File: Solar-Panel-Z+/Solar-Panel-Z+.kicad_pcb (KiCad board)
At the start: 6 copper layers, 48.4 x 48.4 mm, 79 parts, among them J1 FTS-105-01-L-DV-A, Q1 BSS138DWQ-7, Q2 MBT2222ADW1T1, Q3 BSS138DWQ-7, Q4 MBT2222ADW1T1, U1 BQ25570RGRR, U2 TSL2561

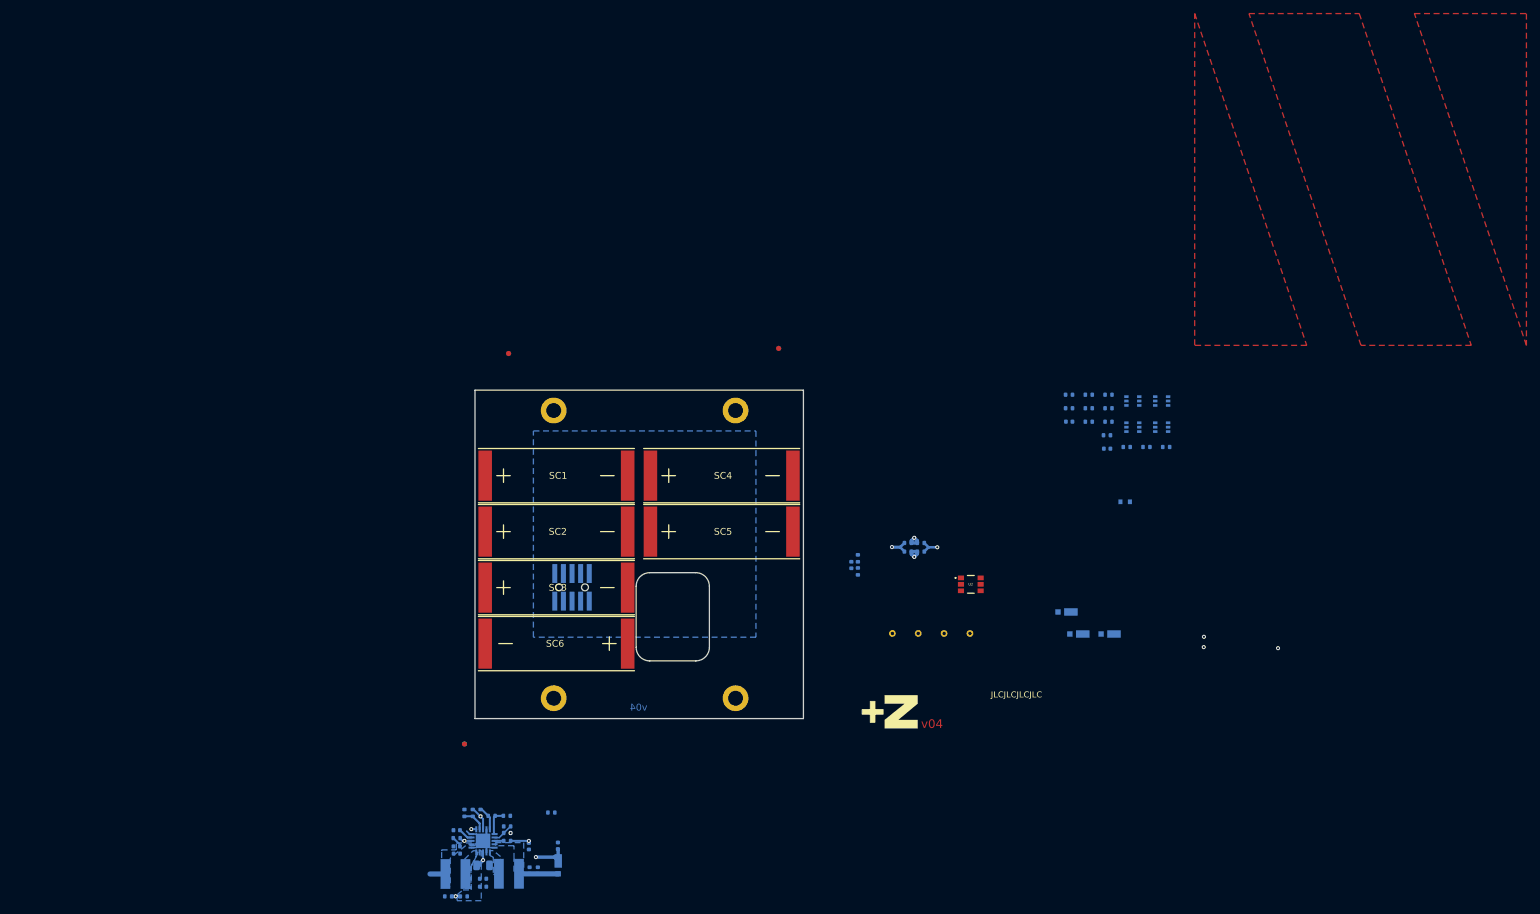
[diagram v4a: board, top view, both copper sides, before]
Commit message: Finish 6 Layer panel versions
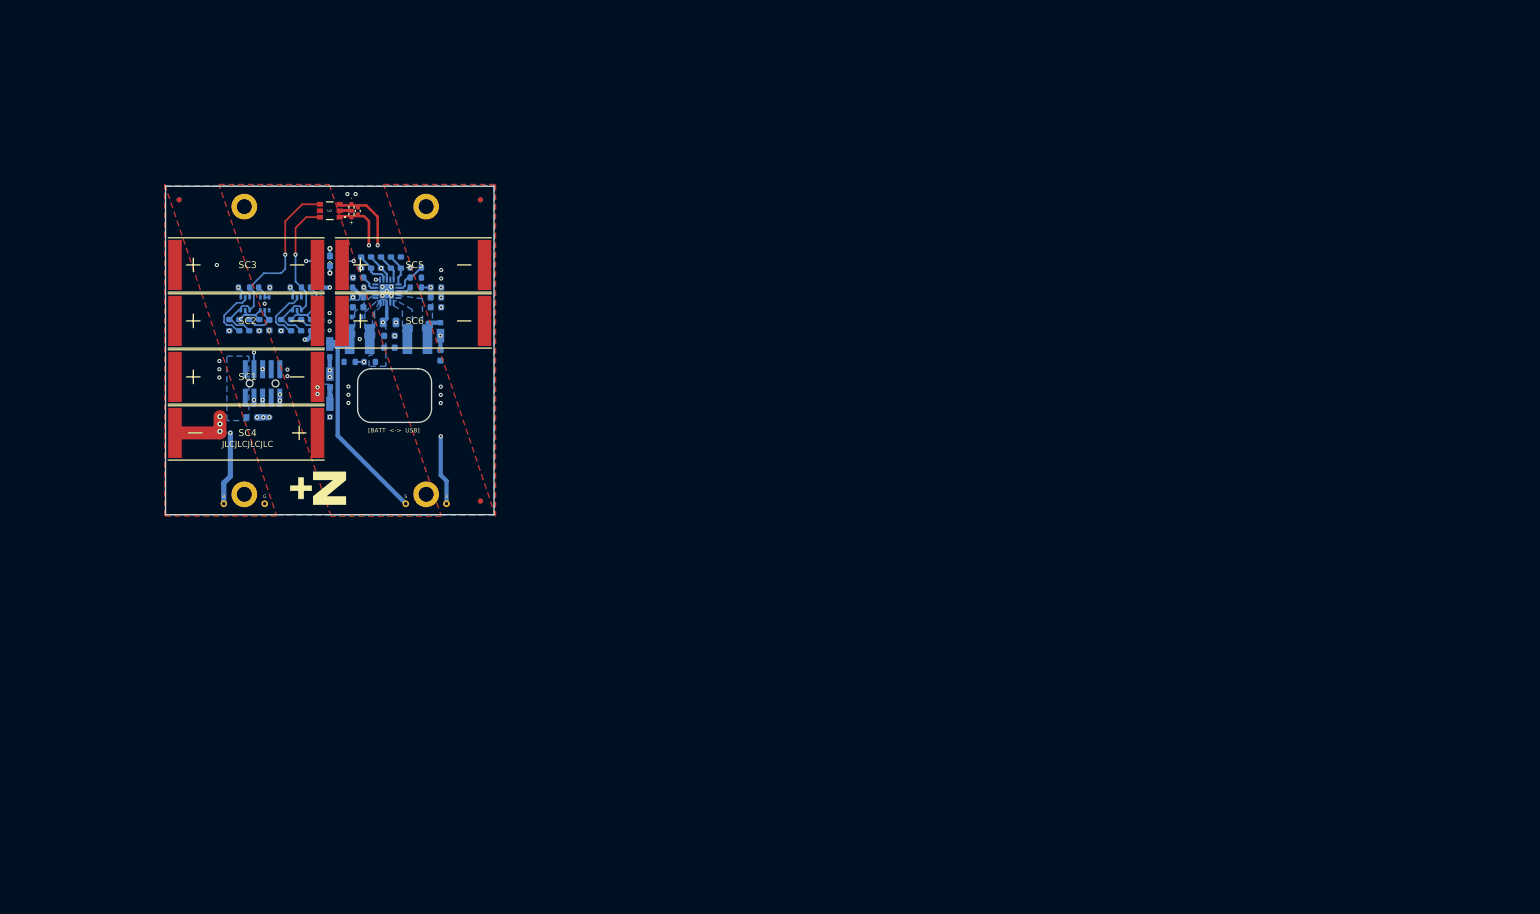
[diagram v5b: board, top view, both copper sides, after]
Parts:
- removed the C1 at (183.6, 98.1)
- removed R31: 200K, Resistor_SMD:R_0402_1005Metric
- removed the REF** at (133.1, 67.0) (x2)
- removed the REF** at (126.5, 124.5) (x2)
- removed the REF** at (172.8, 66.2) (x2)
- removed the Ref** at (143.9, 115.2)
- added C5: 100uF, Capacitor_SMD:C_0805_2012Metric, B.Cu at (115.5, 62.4)
- added R4: 0, Resistor_SMD:R_0603_1608Metric, B.Cu at (119.4, 57.2)
- added REF**: Fiducial_0.75mm_Mask1.5mm, Fiducial:Fiducial_0.75mm_Mask1.5mm, F.Cu at (128.9, 88.7)
- added REF**: Fiducial_0.75mm_Mask1.5mm, Fiducial:Fiducial_0.75mm_Mask1.5mm, F.Cu at (84.5, 44.3)
- added REF**: Fiducial_0.75mm_Mask1.5mm, Fiducial:Fiducial_0.75mm_Mask1.5mm, F.Cu at (128.9, 44.3)
- added REF**: Fiducial_0.75mm_Mask1.5mm, Fiducial:Fiducial_0.75mm_Mask1.5mm, B.Cu at (128.9, 44.3)
- added REF**: Fiducial_0.75mm_Mask1.5mm, Fiducial:Fiducial_0.75mm_Mask1.5mm, B.Cu at (84.5, 44.3)
- added REF**: Fiducial_0.75mm_Mask1.5mm, Fiducial:Fiducial_0.75mm_Mask1.5mm, B.Cu at (128.9, 88.7)
- added Ref**: Val**, custom-footprints:pycubed_mini_half, B.Cu at (106.2, 44.6)
- C1: renamed from C5; value 100uF -> 1uF; footprint Capacitor_SMD:C_0805_2012Metric -> Capacitor_SMD:C_0402_1005Metric; moved to F.Cu
- C10, C11, C12, C13, C2, C3, C4, C6, C7, C8, C9: footprint Capacitor_SMD:C_0402_1005Metric -> Capacitor_SMD:C_0603_1608Metric
- H1, H2, H3, H4: moved to B.Cu
- J1: footprint batteryboard:FTS-105-XX-YY-DV-A -> solarpanels:SAMTEC-FTS-105-01-X-DV-A
- R1, R2: moved to F.Cu
- R10, R11, R12, R13, R16, R17, R18, R24, R29, R3, R5, R6, R7, R8, R9: footprint Resistor_SMD:R_0402_1005Metric -> Resistor_SMD:R_0603_1608Metric
- R14, R15, R19: value 0 -> DNI; footprint Resistor_SMD:R_0402_1005Metric -> Resistor_SMD:R_0603_1608Metric
- R20: value 680 -> DNI; footprint Resistor_SMD:R_0402_1005Metric -> Resistor_SMD:R_0603_1608Metric
- R21: value 100K -> 680; footprint Resistor_SMD:R_0402_1005Metric -> Resistor_SMD:R_0603_1608Metric
- R22: value 0 -> 100K; footprint Resistor_SMD:R_0402_1005Metric -> Resistor_SMD:R_0603_1608Metric
- R23: value 0 -> 10K; footprint Resistor_SMD:R_0402_1005Metric -> Resistor_SMD:R_0603_1608Metric
- R25, R30: value 10K -> 200K; footprint Resistor_SMD:R_0402_1005Metric -> Resistor_SMD:R_0603_1608Metric
- R26: value 200K -> 680; footprint Resistor_SMD:R_0402_1005Metric -> Resistor_SMD:R_0603_1608Metric
- R27: value 680 -> 100K; footprint Resistor_SMD:R_0402_1005Metric -> Resistor_SMD:R_0603_1608Metric
- R28: value 100K -> 10K; footprint Resistor_SMD:R_0402_1005Metric -> Resistor_SMD:R_0603_1608Metric
- SC1, SC2, SC3, SC4, SC5, SC6: value SolarCell -> SolarCell_Small
- moved R21 137.8 mm to (93.4, 62.8), turned to 90 degrees
- moved Q1 133.4 mm to (97.1, 59.6), turned to -90 degrees
- moved Q2 132.1 mm to (94.2, 59.6), turned to -90 degrees
- moved R24 130.0 mm to (91.9, 62.8), turned to 90 degrees
- moved Q4 128.2 mm to (101.9, 59.6), turned to -90 degrees
- moved R22 126.1 mm to (97.0, 57.2)
- moved R20 124.7 mm to (101.7, 57.2)
- moved R23 122.9 mm to (96.3, 62.8), turned to 90 degrees
- moved R29 122.6 mm to (99.5, 62.8), turned to 90 degrees
- moved R25 121.4 mm to (94.8, 62.8), turned to 90 degrees
- moved Q3 121.1 mm to (104.8, 59.6), turned to -90 degrees
- moved D3 119.6 mm to (106.7, 75.1), turned to -90 degrees
- moved C12 118.7 mm to (97.8, 62.8), turned to -90 degrees
- moved R28 118.4 mm to (104.0, 62.8), turned to 90 degrees
- moved D5 118.1 mm to (106.7, 66.2), turned to -90 degrees
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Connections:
- C1 pad 1: VBAT -> GND
- C1 pad 2: GND -> +3V3
- J1 pad 10: VUSB -> BATT_P
- J1 pad 4: BURN2 -> GND
- J1 pad 7: SDA2 -> SDA
- J1 pad 8: SCL2 -> SCL
- Q2 pad 1: SCL2 -> SCL
- Q2 pad 3: SCL2 -> SCL
- Q4 pad 1: SDA2 -> SDA
- Q4 pad 3: SDA2 -> SDA
- R19 pad 1: VBAT_OK -> SCL_LS
- R19 pad 2: VOUT_EN -> SCL
- R20 pad 1: Net-(Q2-Pad2) -> SDA_LS
- R20 pad 2: Net-(Q1-Pad6) -> SDA
- R21 pad 1: +3V3 -> Net-(Q2-Pad2)
- R21 pad 2: Net-(Q1-Pad2) -> Net-(Q1-Pad6)
- R22 pad 1: SCL_LS -> +3V3
- R22 pad 2: SCL2 -> Net-(Q1-Pad2)
- R23 pad 1: SDA_LS -> +3V3
- R23 pad 2: SDA2 -> Net-(Q1-Pad6)
- R24 pad 2: Net-(Q1-Pad6) -> SCL_LS
- R25 pad 1: +3V3 -> SCL_LS
- R25 pad 2: SCL_LS -> Net-(C12-Pad1)
- R26 pad 1: SCL_LS -> Net-(Q4-Pad2)
- R26 pad 2: Net-(C12-Pad1) -> Net-(Q3-Pad6)
- R27 pad 1: Net-(Q4-Pad2) -> +3V3
- R27 pad 2: Net-(Q3-Pad6) -> Net-(Q3-Pad2)
- R28 pad 2: Net-(Q3-Pad2) -> Net-(Q3-Pad6)
- R29 pad 2: Net-(Q3-Pad6) -> SDA_LS
- R30 pad 1: +3V3 -> SDA_LS
- R30 pad 2: SDA_LS -> Net-(C13-Pad1)
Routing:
- net GND: track 13526.1 -> 20.8 mm, vias 3 -> 34
- net /coil: track 7.26 -> 13196.6 mm, vias 2 -> 5
- net SCL_LS: track 0.00 -> 31.3 mm, vias 0 -> 1
- net VSOLAR: track 3.89 -> 32.7 mm
- net SDA_LS: track 0.00 -> 25.8 mm, vias 0 -> 1
- net /VSOLAR_FULL: track 0.00 -> 24.4 mm, vias 0 -> 5
- net SDA: track 0.00 -> 24.0 mm, vias 0 -> 2
- net COIL_P: track 2.83 -> 23.8 mm, vias 1 -> 2
- net COIL_N: track 2.78 -> 23.0 mm, vias 1 -> 2
- net +3V3: track 5.29 -> 23.6 mm, vias 1 -> 11
- net SCL: track 0.00 -> 16.9 mm, vias 0 -> 2
- net VBAT: track 2.11 -> 16.9 mm, vias 1 -> 5
- net Net-(R14-Pad1): track 3.14 -> 14.8 mm
- net Net-(Q2-Pad2): track 0.00 -> 7.92 mm
- net Net-(Q4-Pad2): track 0.00 -> 7.84 mm
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- added copper zone on In3.Cu, net +3V3
- added copper zone on B.Cu, net BATT_P
- added copper zone on In1.Cu, net GND
- added copper zone on In4.Cu, net GND
- added copper zone on B.Cu, net Net-(D3-Pad1)
- added copper zone on In2.Cu, net VBAT
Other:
- outline, holes or cut-outs redrawn
- board text added: "1.3V3 3.BURN1 5.COIL_P 7.SDA 9.BATT_P"
- board text added: "2.GND 4.GND 6.COIL_N 8.SCL 10.BATT_P"
- board text added: "3"
- board text added: "B"
- board text added: "G"
- board text added: "Rev B2/01"
- board text added: "S"
- board text added: "VBAT"
- board text added: "[BATT <-> USB]"
- board text added: "^"
- board text added: "⊗"
- board text added: "⊙"
- board text removed: "BATT_P"
- board text removed: "Cable Pinout 1.BATT_P 2.BATT_N 3.SDA 4.SCL 5.BURN 6.3V3 7.GND 8.GND 9.COIL_N 10.COIL_P"
- board text removed: "v04"
